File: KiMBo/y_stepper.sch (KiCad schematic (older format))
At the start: 25 parts, among them U24 TMC2130

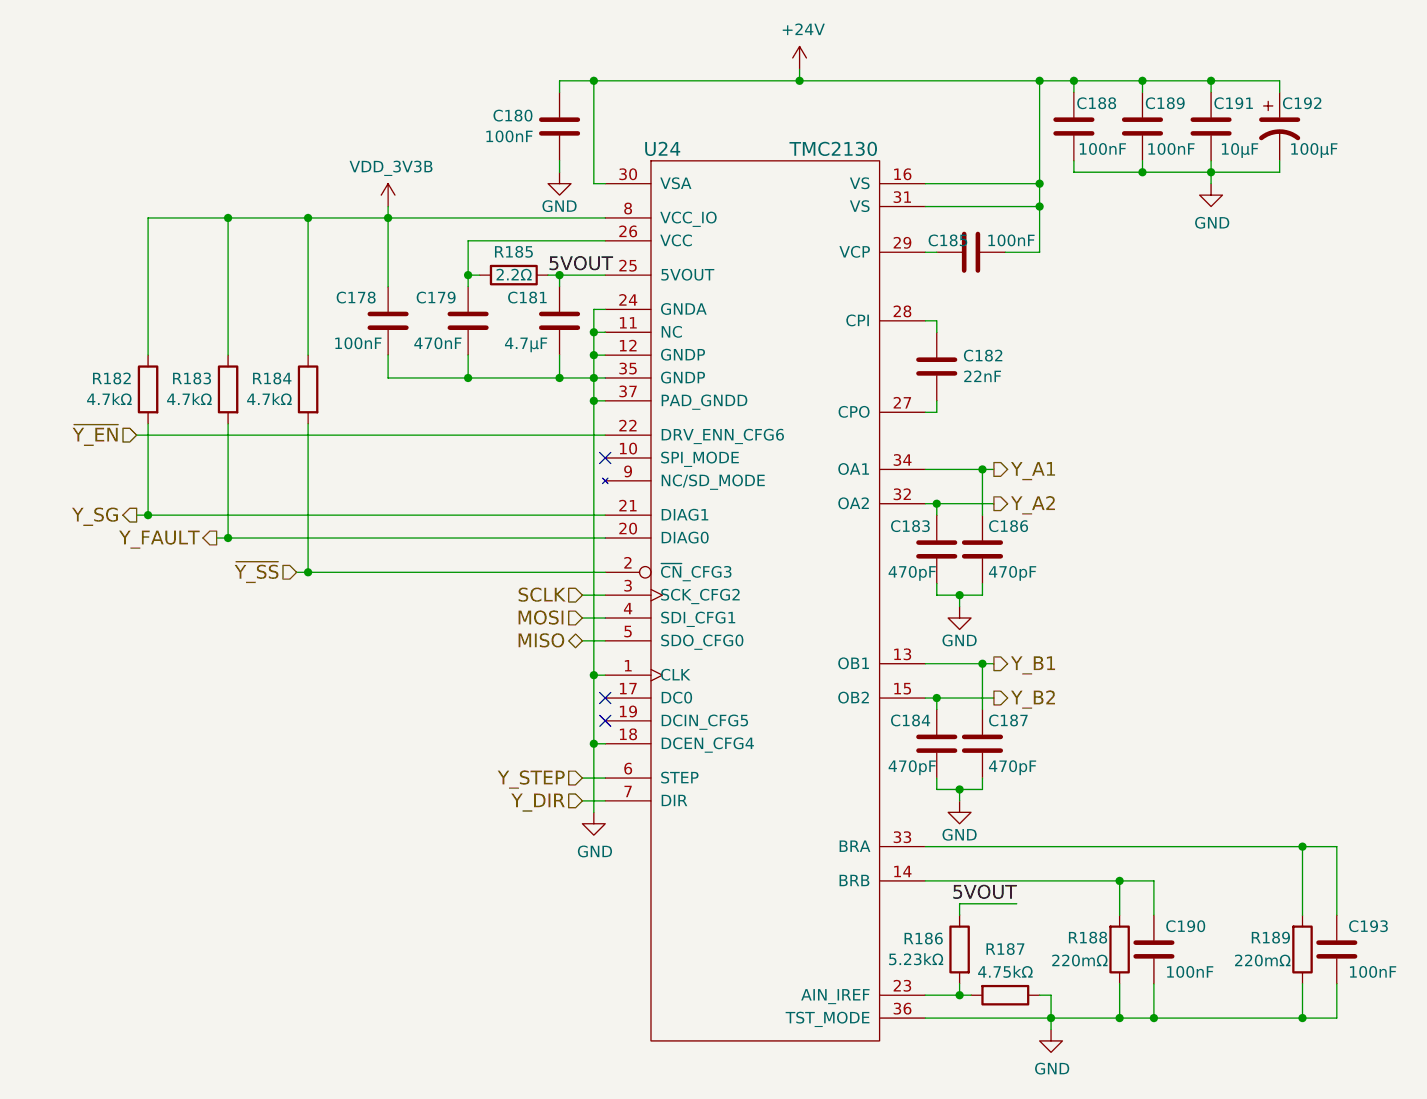
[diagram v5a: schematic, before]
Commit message: Begin layout
Arrange all connectors to get a feel for the area.
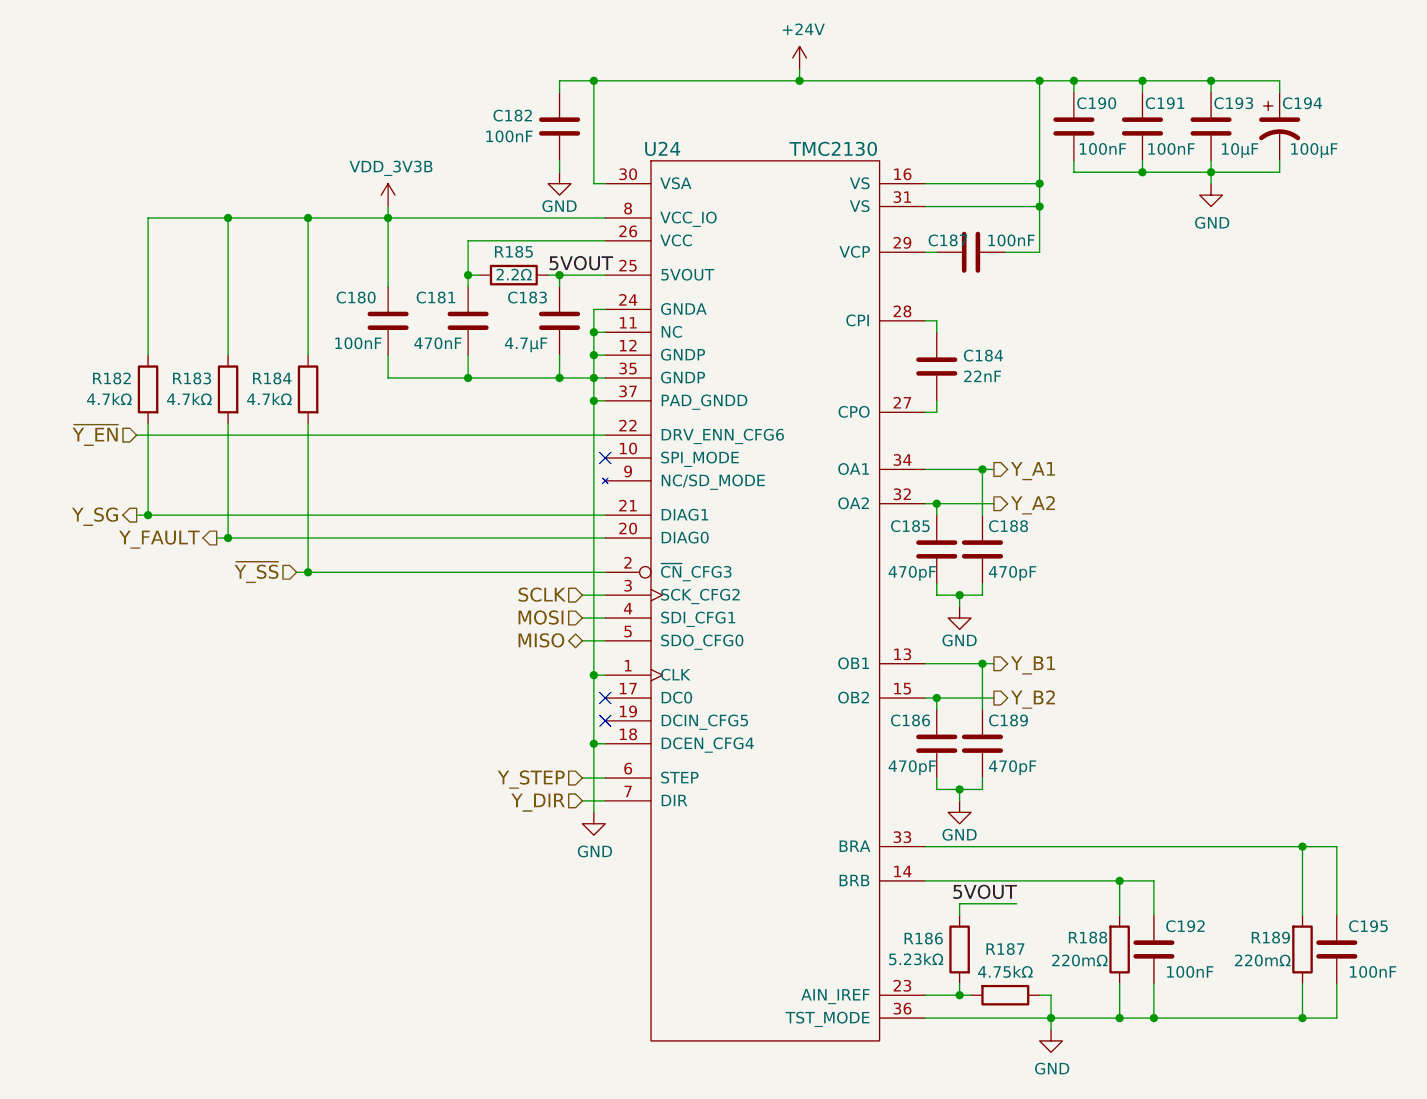
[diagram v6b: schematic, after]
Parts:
- renumbered C178 to C180, C179 to C181, C180 to C182, C181 to C183, C182 to C184, C183 to C185, C184 to C186, C185 to C187, C186 to C188, C187 to C189, C188 to C190, C189 to C191, C190 to C192, C191 to C193, C192 to C194, C193 to C195
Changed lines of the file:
@@
 Y_SG
 $Comp
-L C C180
+L C C182
 U 1 1 58C0B215
 P 6550 3250
-F 0 "C180" H 6436 3204 50  0000 R CNN
+F 0 "C182" H 6436 3204 50  0000 R CNN
 F 1 "100nF" H 6436 3295 50  0000 R CNN
 F 2 "Capacitors_SMD:C_0603" H 6588 3100 50  0001 C CNN
@@
 $EndComp
 $Comp
-L C C185
+L C C187
 U 1 1 58C0B21C
 P 8350 3800
-F 0 "C185" V 8300 3700 50  0000 C CNN
+F 0 "C187" V 8300 3700 50  0000 C CNN
 F 1 "100nF" V 8300 3975 50  0000 C CNN
 F 2 "Capacitors_SMD:C_0603" H 8388 3650 50  0001 C CNN
@@
 $EndComp
 $Comp
-L CP1 C192
+L CP1 C194
 U 1 1 58C0B223
 P 9700 3250
-F 0 "C192" H 9800 3350 50  0000 C CNN
+F 0 "C194" H 9800 3350 50  0000 C CNN
 F 1 "100μF" H 9850 3150 50  0000 C CNN
 F 2 "Capacitors_SMD:c_elec_8x10" H 9700 3250 50  0001 C CNN
@@
 $EndComp
 $Comp
-L C C188
+L C C190
 U 1 1 58C0B22A
 P 8800 3250
-F 0 "C188" H 8700 3350 50  0000 C CNN
+F 0 "C190" H 8700 3350 50  0000 C CNN
 F 1 "100nF" H 8675 3150 50  0000 C CNN
 F 2 "Capacitors_SMD:C_0603" H 8838 3100 50  0001 C CNN
@@
 $EndComp
 $Comp
-L GND #PWR0245
+L GND #PWR0248
 U 1 1 58C0B231
 P 6550 3450
-F 0 "#PWR0245" H 6550 3200 50  0001 C CNN
+F 0 "#PWR0248" H 6550 3200 50  0001 C CNN
 F 1 "GND" H 6550 3300 50  0000 C CNN
 F 2 "" H 6550 3450 50  0000 C CNN
@@
 $EndComp
 $Comp
-L C C189
+L C C191
 U 1 1 58C0B237
 P 9100 3250
-F 0 "C189" H 9000 3350 50  0000 C CNN
+F 0 "C191" H 9000 3350 50  0000 C CNN
 F 1 "100nF" H 8975 3150 50  0000 C CNN
 F 2 "Capacitors_SMD:C_0603" H 9138 3100 50  0001 C CNN
@@
 $EndComp
 $Comp
-L GND #PWR0246
+L GND #PWR0249
 U 1 1 58C0B23E
 P 9400 3500
-F 0 "#PWR0246" H 9400 3250 50  0001 C CNN
+F 0 "#PWR0249" H 9400 3250 50  0001 C CNN
 F 1 "GND" H 9405 3327 50  0000 C CNN
 F 2 "" H 9400 3500 50  0000 C CNN
@@
 $EndComp
 $Comp
-L +24V #PWR0247
+L +24V #PWR0250
 U 1 1 58C0B244
 P 7600 3000
-F 0 "#PWR0247" H 7600 2850 50  0001 C CNN
+F 0 "#PWR0250" H 7600 2850 50  0001 C CNN
 F 1 "+24V" H 7615 3173 50  0000 C CNN
 F 2 "" H 7600 3000 50  0000 C CNN
@@
 $EndComp
 $Comp
-L C C182
+L C C184
 U 1 1 58C0B24A
 P 8200 4300
-F 0 "C182" H 8315 4346 50  0000 L CNN
+F 0 "C184" H 8315 4346 50  0000 L CNN
 F 1 "22nF" H 8315 4255 50  0000 L CNN
 F 2 "Capacitors_SMD:C_0603" H 8238 4150 50  0001 C CNN
@@
 $EndComp
 $Comp
-L GND #PWR0248
+L GND #PWR0251
 U 1 1 58C0B25F
 P 8700 7200
-F 0 "#PWR0248" H 8700 6950 50  0001 C CNN
+F 0 "#PWR0251" H 8700 6950 50  0001 C CNN
 F 1 "GND" H 8705 7027 50  0000 C CNN
 F 2 "" H 8700 7200 50  0000 C CNN
@@
 $EndComp
 $Comp
-L C C179
+L C C181
 U 1 1 58C0B26D
 P 6150 4100
-F 0 "C179" H 6200 4200 50  0000 L CNN
+F 0 "C181" H 6200 4200 50  0000 L CNN
 F 1 "470nF" H 6175 4000 50  0000 L CNN
 F 2 "Capacitors_SMD:C_0603" H 6188 3950 50  0001 C CNN
@@
 NoConn ~ 6750 5850
 $Comp
-L GND #PWR0249
+L GND #PWR0252
 U 1 1 58C0B282
 P 6700 6250
-F 0 "#PWR0249" H 6700 6000 50  0001 C CNN
+F 0 "#PWR0252" H 6700 6000 50  0001 C CNN
 F 1 "GND" H 6705 6077 50  0000 C CNN
 F 2 "" H 6700 6250 50  0000 C CNN
@@
 $EndComp
 $Comp
-L C C190
+L C C192
 U 1 1 58C0B288
 P 9150 6850
-F 0 "C190" H 9200 6950 50  0000 L CNN
+F 0 "C192" H 9200 6950 50  0000 L CNN
 F 1 "100nF" H 9200 6750 50  0000 L CNN
 F 2 "Capacitors_SMD:C_0603" H 9188 6700 50  0001 C CNN
@@
 NoConn ~ 6750 4700
 $Comp
-L C C181
+L C C183
 U 1 1 58C0B29A
 P 6550 4100
-F 0 "C181" H 6600 4200 50  0000 L CNN
+F 0 "C183" H 6600 4200 50  0000 L CNN
 F 1 "4.7μF" H 6600 4000 50  0000 L CNN
 F 2 "Capacitors_SMD:C_0603" H 6588 3950 50  0001 C CNN
@@
 $EndComp
 $Comp
-L C C193
+L C C195
 U 1 1 58C0B2B8
 P 9950 6850
-F 0 "C193" H 10000 6950 50  0000 L CNN
+F 0 "C195" H 10000 6950 50  0000 L CNN
 F 1 "100nF" H 10000 6750 50  0000 L CNN
 F 2 "Capacitors_SMD:C_0603" H 9988 6700 50  0001 C CNN
@@
 $EndComp
 $Comp
-L C C183
+L C C185
 U 1 1 58C0B2BF
 P 8200 5100
-F 0 "C183" H 8225 5200 50  0000 L CNN
+F 0 "C185" H 8225 5200 50  0000 L CNN
 F 1 "470pF" H 8200 5000 50  0000 L CNN
 F 2 "Capacitors_SMD:C_0603" H 8238 4950 50  0001 C CNN
@@
 $EndComp
 $Comp
-L GND #PWR0250
+L GND #PWR0253
 U 1 1 58C0B2C6
 P 8300 5350
-F 0 "#PWR0250" H 8300 5100 50  0001 C CNN
+F 0 "#PWR0253" H 8300 5100 50  0001 C CNN
 F 1 "GND" H 8300 5200 50  0000 C CNN
 F 2 "" H 8300 5350 50  0000 C CNN
@@
 $EndComp
 $Comp
-L C C186
+L C C188
 U 1 1 58C0B2CC
 P 8400 5100
-F 0 "C186" H 8425 5200 50  0000 L CNN
+F 0 "C188" H 8425 5200 50  0000 L CNN
 F 1 "470pF" H 8425 5000 50  0000 L CNN
 F 2 "Capacitors_SMD:C_0603" H 8438 4950 50  0001 C CNN
@@
 $EndComp
 $Comp
-L C C184
+L C C186
 U 1 1 58C0B2D3
 P 8200 5950
-F 0 "C184" H 8225 6050 50  0000 L CNN
+F 0 "C186" H 8225 6050 50  0000 L CNN
 F 1 "470pF" H 8200 5850 50  0000 L CNN
 F 2 "Capacitors_SMD:C_0603" H 8238 5800 50  0001 C CNN
@@
 $EndComp
 $Comp
-L GND #PWR0251
+L GND #PWR0254
 U 1 1 58C0B2DA
 P 8300 6200
-F 0 "#PWR0251" H 8300 5950 50  0001 C CNN
+F 0 "#PWR0254" H 8300 5950 50  0001 C CNN
 F 1 "GND" H 8300 6050 50  0000 C CNN
 F 2 "" H 8300 6200 50  0000 C CNN
@@
 $EndComp
 $Comp
-L C C187
+L C C189
 U 1 1 58C0B2E0
 P 8400 5950
-F 0 "C187" H 8425 6050 50  0000 L CNN
+F 0 "C189" H 8425 6050 50  0000 L CNN
 F 1 "470pF" H 8425 5850 50  0000 L CNN
 F 2 "Capacitors_SMD:C_0603" H 8438 5800 50  0001 C CNN
@@
 Connection ~ 5100 3650
 $Comp
-L C C191
+L C C193
 U 1 1 58C0B366
 P 9400 3250
-F 0 "C191" H 9300 3350 50  0000 C CNN
+F 0 "C193" H 9300 3350 50  0000 C CNN
 F 1 "10μF" H 9275 3150 50  0000 C CNN
 F 2 "Capacitors_SMD:C_0805" H 9438 3100 50  0001 C CNN
@@
 	4750 3650 6750 3650
 $Comp
-L VDD_3V3B #PWR0252
+L VDD_3V3B #PWR0255
 U 1 1 5A300CA5
 P 5800 3600
-F 0 "#PWR0252" H 5800 3450 50  0001 C CNN
+F 0 "#PWR0255" H 5800 3450 50  0001 C CNN
 F 1 "VDD_3V3B" H 5815 3773 50  0000 C CNN
 F 2 "" H 5800 3600 50  0000 C CNN
@@
 $EndComp
 $Comp
-L C C178
+L C C180
 U 1 1 5A89AE9E
 P 5800 4100
-F 0 "C178" H 5850 4200 50  0000 L CNN
+F 0 "C180" H 5850 4200 50  0000 L CNN
 F 1 "100nF" H 5825 4000 50  0000 L CNN
 F 2 "Capacitors_SMD:C_0603" H 5838 3950 50  0001 C CNN

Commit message: Arrange connectors and E-stepper circuit
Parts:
- R187: footprint Resistors_SMD:R_0805 -> Resistors_SMD:R_0603
- R189: footprint Resistors_SMD:R_0603 -> Resistors_SMD:R_0805
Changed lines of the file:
@@
 F 0 "R189" H 9750 6800 50  0000 R CNN
 F 1 "220mΩ" H 9750 6900 50  0000 R CNN
-F 2 "Resistors_SMD:R_0603" V 9730 6850 50  0001 C CNN
+F 2 "Resistors_SMD:R_0805" V 9730 6850 50  0001 C CNN
 F 3 "" H 9800 6850 50  0000 C CNN
 	1    9800 6850
@@
 F 0 "R187" V 8300 7050 50  0000 C CNN
 F 1 "4.75kΩ" V 8400 7050 50  0000 C CNN
-F 2 "Resistors_SMD:R_0805" V 8430 7050 50  0001 C CNN
+F 2 "Resistors_SMD:R_0603" V 8430 7050 50  0001 C CNN
 F 3 "" H 8500 7050 50  0000 C CNN
 	1    8500 7050
